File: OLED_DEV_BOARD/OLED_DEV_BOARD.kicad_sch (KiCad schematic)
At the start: 32 parts, among them J1 Barrel_Jack, J2 Conn_02x10_Odd_Even, J3 AudioJack3_Ground, J4 Conn_02x20_Odd_Even, SW1 SW_DIP_x02, SW2 SW_MEC_5E, SW3 SW_MEC_5E, SW4 SW_MEC_5E, SW5 SW_MEC_5E, SW6 SW_MEC_5E, SW7 SW_MEC_5E, U1 IS66WVS1M8BLL-104NLI, U2 W25Q32JVSS, U3 NCP1117-3.3_TO252

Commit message: Added proper footprint for OLED module and placed components roughly
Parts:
- J2: footprint Connector_PinHeader_2.54mm:PinHeader_2x10_P2.54mm_Vertical -> OLED:NHD-1.8-160128UBC3
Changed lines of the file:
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@@
     (property "Reference" "J2" (id 0) (at 49.53 30.5902 0))
     (property "Value" "Conn_02x10_Odd_Even" (id 1) (at 49.53 33.1271 0))
-    (property "Footprint" "Connector_PinHeader_2.54mm:PinHeader_2x10_P2.54mm_Vertical" (id 2) (at 48.26 45.72 0)
+    (property "Footprint" "OLED:NHD-1.8-160128UBC3" (id 2) (at 48.26 45.72 0)
       (effects (font (size 1.27 1.27)) hide)
     )
@@
     )
     (path "/a17904b9-135e-4dae-ae20-401c7787de72"
-      (reference "J2") (unit 1) (value "Conn_02x10_Odd_Even") (footprint "Connector_PinHeader_2.54mm:PinHeader_2x10_P2.54mm_Vertical")
+      (reference "J2") (unit 1) (value "Conn_02x10_Odd_Even") (footprint "OLED:NHD-1.8-160128UBC3")
     )
     (path "/97d5cdb2-e749-4919-9dcf-4b58ea280295"

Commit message: Made board smaller
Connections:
- net FLASH_CLK: now also J4.36 (Pin_36); no longer J4.32 (Pin_32)
- net FLASH_CSb: now also J4.32 (Pin_32); no longer J4.31 (Pin_31)
- net FLASH_D1: now also J4.31 (Pin_31); no longer J4.34 (Pin_34)
- net FLASH_D2: now also J4.34 (Pin_34); no longer J4.35 (Pin_35)
- net FLASH_D3: now also J4.35 (Pin_35); no longer J4.36 (Pin_36)
- net PSRAM_CLK: now also J4.24 (Pin_24); no longer J4.20 (Pin_20)
- net PSRAM_CSb: now also J4.20 (Pin_20); no longer J4.19 (Pin_19)
- net PSRAM_D1: now also J4.19 (Pin_19); no longer J4.22 (Pin_22)
- net PSRAM_D2: now also J4.22 (Pin_22); no longer J4.23 (Pin_23)
- net PSRAM_D3: now also J4.23 (Pin_23); no longer J4.24 (Pin_24)
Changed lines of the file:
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@@
-    (effects (font (size 1.27 1.27)) (justify left bottom))
-  )
-  (label "PSRAM_D2" (at 163.83 66.04 0)
     (effects (font (size 1.27 1.27)) (justify left bottom))
   )
@@
     (effects (font (size 1.27 1.27)) (justify left bottom))
   )
-  (label "GND" (at 30.48 35.56 0)
+  (label "PSRAM_CLK" (at 228.6 66.04 0)
     (effects (font (size 1.27 1.27)) (justify left bottom))
   )
-  (label "PSRAM_CSb" (at 163.83 60.96 0)
+  (label "FLASH_D3" (at 163.83 81.28 0)
+    (effects (font (size 1.27 1.27)) (justify left bottom))
+  )
+  (label "GND" (at 30.48 35.56 0)
     (effects (font (size 1.27 1.27)) (justify left bottom))
   )
@@
   )
   (label "DB7" (at 228.6 53.34 0)
+    (effects (font (size 1.27 1.27)) (justify left bottom))
+  )
+  (label "PSRAM_D1" (at 163.83 60.96 0)
     (effects (font (size 1.27 1.27)) (justify left bottom))
   )
@@
     (effects (font (size 1.27 1.27)) (justify left bottom))
   )
-  (label "FLASH_D3" (at 223.52 81.28 0)
-    (effects (font (size 1.27 1.27)) (justify left bottom))
-  )
   (label "RIGHT_BUTTON" (at 215.9 134.62 0)
     (effects (font (size 1.27 1.27)) (justify left bottom))
@@
     (effects (font (size 1.27 1.27)) (justify left bottom))
   )
-  (label "BS2" (at 144.78 68.58 0)
+  (label "PSRAM_D2" (at 228.6 63.5 0)
     (effects (font (size 1.27 1.27)) (justify left bottom))
   )
-  (label "PSRAM_CLK" (at 223.52 60.96 0)
+  (label "BS2" (at 144.78 68.58 0)
     (effects (font (size 1.27 1.27)) (justify left bottom))
   )
@@
     (effects (font (size 1.27 1.27)) (justify left bottom))
   )
+  (label "FLASH_CLK" (at 223.52 81.28 0)
+    (effects (font (size 1.27 1.27)) (justify left bottom))
+  )
   (label "DOWN_BUTTON" (at 223.52 71.12 0)
     (effects (font (size 1.27 1.27)) (justify left bottom))
@@
     (effects (font (size 1.27 1.27)) (justify left bottom))
   )
+  (label "FLASH_D1" (at 163.83 76.2 0)
+    (effects (font (size 1.27 1.27)) (justify left bottom))
+  )
   (label "FLASH_CSb" (at 26.67 115.57 0)
     (effects (font (size 1.27 1.27)) (justify left bottom))
   )
-  (label "PSRAM_D1" (at 223.52 63.5 0)
+  (label "PSRAM_D3" (at 163.83 66.04 0)
     (effects (font (size 1.27 1.27)) (justify left bottom))
   )
   (label "PSRAM_D3" (at 64.77 86.36 0)
-    (effects (font (size 1.27 1.27)) (justify left bottom))
-  )
-  (label "PSRAM_D3" (at 223.52 66.04 0)
     (effects (font (size 1.27 1.27)) (justify left bottom))
   )
@@
     (effects (font (size 1.27 1.27)) (justify left bottom))
   )
-  (label "FLASH_D1" (at 223.52 78.74 0)
-    (effects (font (size 1.27 1.27)) (justify left bottom))
-  )
   (label "DB6" (at 29.21 50.8 0)
-    (effects (font (size 1.27 1.27)) (justify left bottom))
-  )
-  (label "FLASH_CSb" (at 163.83 76.2 0)
     (effects (font (size 1.27 1.27)) (justify left bottom))
   )
@@
   )
   (label "UP_BUTTON" (at 191.77 118.11 0)
-    (effects (font (size 1.27 1.27)) (justify left bottom))
-  )
-  (label "FLASH_D2" (at 163.83 81.28 0)
     (effects (font (size 1.27 1.27)) (justify left bottom))
   )
@@
     (effects (font (size 1.27 1.27)) (justify left bottom))
   )
+  (label "FLASH_D2" (at 223.52 78.74 0)
+    (effects (font (size 1.27 1.27)) (justify left bottom))
+  )
   (label "DB2" (at 163.83 48.26 0)
     (effects (font (size 1.27 1.27)) (justify left bottom))
   )
   (label "E" (at 163.83 43.18 0)
-    (effects (font (size 1.27 1.27)) (justify left bottom))
-  )
-  (label "FLASH_CLK" (at 223.52 76.2 0)
     (effects (font (size 1.27 1.27)) (justify left bottom))
   )
@@
     (effects (font (size 1.27 1.27)) (justify left bottom))
   )
+  (label "FLASH_CSb" (at 223.52 76.2 0)
+    (effects (font (size 1.27 1.27)) (justify left bottom))
+  )
   (label "DB4" (at 29.21 48.26 0)
     (effects (font (size 1.27 1.27)) (justify left bottom))
@@
     (effects (font (size 1.27 1.27)) (justify left bottom))
   )
+  (label "PSRAM_CSb" (at 228.6 60.96 0)
+    (effects (font (size 1.27 1.27)) (justify left bottom))
+  )

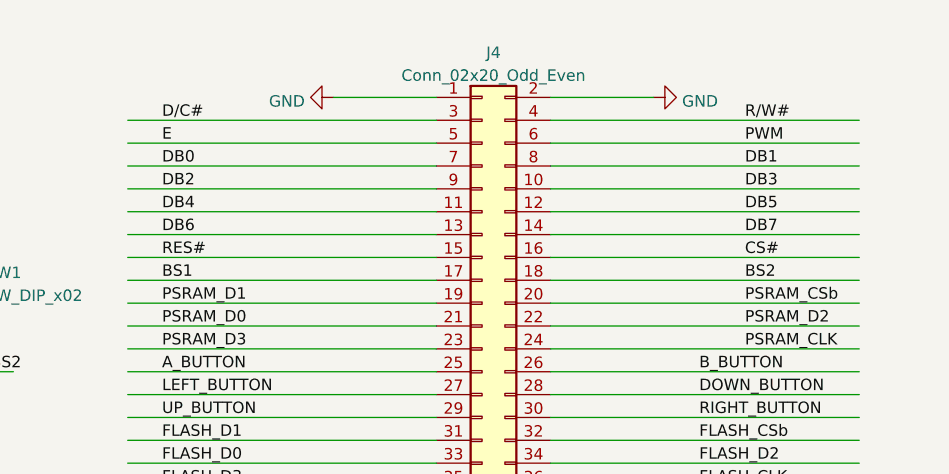
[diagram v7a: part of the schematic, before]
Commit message: Changed ordering of pins for display so it would route better
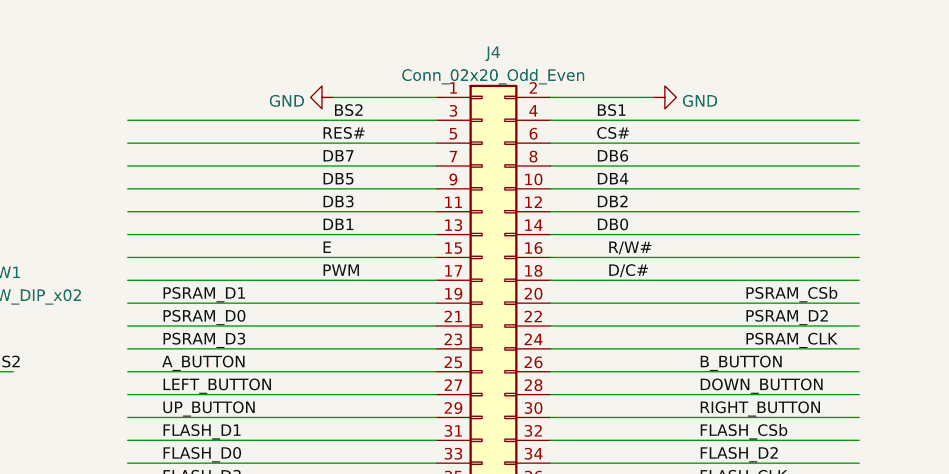
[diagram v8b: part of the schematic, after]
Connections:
- net BS1: now also J4.4 (Pin_4); no longer J4.17 (Pin_17)
- net BS2: now also J4.3 (Pin_3); no longer J4.18 (Pin_18)
- net CS#: now also J4.6 (Pin_6); no longer J4.16 (Pin_16)
- net DB0: now also J4.14 (Pin_14); no longer J4.7 (Pin_7)
- net DB1: now also J4.13 (Pin_13); no longer J4.8 (Pin_8)
- net DB2: now also J4.12 (Pin_12); no longer J4.9 (Pin_9)
- net DB3: now also J4.11 (Pin_11); no longer J4.10 (Pin_10)
- net DB4: now also J4.10 (Pin_10); no longer J4.11 (Pin_11)
- net DB5: now also J4.9 (Pin_9); no longer J4.12 (Pin_12)
- net DB6: now also J4.8 (Pin_8); no longer J4.13 (Pin_13)
- net DB7: now also J4.7 (Pin_7); no longer J4.14 (Pin_14)
- net D/C#: now also J4.18 (Pin_18); no longer J4.3 (Pin_3)
- net E: now also J4.15 (Pin_15); no longer J4.5 (Pin_5)
- net PWM: now also J4.17 (Pin_17); no longer J4.6 (Pin_6)
- net RES#: now also J4.5 (Pin_5); no longer J4.15 (Pin_15)
- net R/W#: now also J4.16 (Pin_16); no longer J4.4 (Pin_4)
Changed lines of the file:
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@@
-    (effects (font (size 1.27 1.27)) (justify left bottom))
-  )
-  (label "DB4" (at 163.83 50.8 0)
     (effects (font (size 1.27 1.27)) (justify left bottom))
   )
@@
     (effects (font (size 1.27 1.27)) (justify left bottom))
   )
-  (label "BS2" (at 228.6 58.42 0)
-    (effects (font (size 1.27 1.27)) (justify left bottom))
-  )
-  (label "CS#" (at 228.6 55.88 0)
-    (effects (font (size 1.27 1.27)) (justify left bottom))
-  )
   (label "FLASH_D0" (at 67.31 113.03 0)
     (effects (font (size 1.27 1.27)) (justify left bottom))
@@
     (effects (font (size 1.27 1.27)) (justify left bottom))
   )
-  (label "D{slash}C#" (at 163.83 40.64 0)
-    (effects (font (size 1.27 1.27)) (justify left bottom))
-  )
-  (label "DB7" (at 228.6 53.34 0)
-    (effects (font (size 1.27 1.27)) (justify left bottom))
-  )
   (label "PSRAM_D1" (at 163.83 60.96 0)
     (effects (font (size 1.27 1.27)) (justify left bottom))
@@
     (effects (font (size 1.27 1.27)) (justify left bottom))
   )
+  (label "R{slash}W#" (at 213.36 55.88 0)
+    (effects (font (size 1.27 1.27)) (justify left bottom))
+  )
   (label "RIGHT_BUTTON" (at 215.9 134.62 0)
     (effects (font (size 1.27 1.27)) (justify left bottom))
   )
-  (label "BS1" (at 163.83 58.42 0)
-    (effects (font (size 1.27 1.27)) (justify left bottom))
-  )
-  (label "RES#" (at 163.83 55.88 0)
-    (effects (font (size 1.27 1.27)) (justify left bottom))
-  )
   (label "PSRAM_D2" (at 228.6 63.5 0)
     (effects (font (size 1.27 1.27)) (justify left bottom))
@@
     (effects (font (size 1.27 1.27)) (justify left bottom))
   )
+  (label "DB4" (at 212.09 48.26 0)
+    (effects (font (size 1.27 1.27)) (justify left bottom))
+  )
+  (label "PWM" (at 181.61 58.42 0)
+    (effects (font (size 1.27 1.27)) (justify left bottom))
+  )
   (label "PSRAM_CSb" (at 27.94 83.82 0)
     (effects (font (size 1.27 1.27)) (justify left bottom))
@@
     (effects (font (size 1.27 1.27)) (justify left bottom))
   )
+  (label "DB7" (at 181.61 45.72 0)
+    (effects (font (size 1.27 1.27)) (justify left bottom))
+  )
+  (label "RES#" (at 181.61 43.18 0)
+    (effects (font (size 1.27 1.27)) (justify left bottom))
+  )
   (label "DOWN_BUTTON" (at 223.52 71.12 0)
     (effects (font (size 1.27 1.27)) (justify left bottom))
@@
     (effects (font (size 1.27 1.27)) (justify left bottom))
   )
+  (label "DB1" (at 181.61 53.34 0)
+    (effects (font (size 1.27 1.27)) (justify left bottom))
+  )
   (label "PSRAM_CLK" (at 64.77 88.9 0)
     (effects (font (size 1.27 1.27)) (justify left bottom))
@@
     (effects (font (size 1.27 1.27)) (justify left bottom))
   )
+  (label "E" (at 181.61 55.88 0)
+    (effects (font (size 1.27 1.27)) (justify left bottom))
+  )
   (label "PSRAM_D3" (at 64.77 86.36 0)
     (effects (font (size 1.27 1.27)) (justify left bottom))
@@
     (effects (font (size 1.27 1.27)) (justify left bottom))
   )
+  (label "D{slash}C#" (at 213.36 58.42 0)
+    (effects (font (size 1.27 1.27)) (justify left bottom))
+  )
   (label "DB3" (at 62.23 45.72 0)
     (effects (font (size 1.27 1.27)) (justify left bottom))
@@
     (effects (font (size 1.27 1.27)) (justify left bottom))
   )
-  (label "DB1" (at 228.6 45.72 0)
-    (effects (font (size 1.27 1.27)) (justify left bottom))
-  )
   (label "A_BUTTON" (at 158.75 119.38 0)
     (effects (font (size 1.27 1.27)) (justify left bottom))
@@
     (effects (font (size 1.27 1.27)) (justify left bottom))
   )
-  (label "DB0" (at 163.83 45.72 0)
+  (label "BS1" (at 212.09 40.64 0)
     (effects (font (size 1.27 1.27)) (justify left bottom))
   )
@@
     (effects (font (size 1.27 1.27)) (justify left bottom))
   )
+  (label "DB2" (at 212.09 50.8 0)
+    (effects (font (size 1.27 1.27)) (justify left bottom))
+  )
   (label "DB5" (at 62.23 48.26 0)
     (effects (font (size 1.27 1.27)) (justify left bottom))
   )
-  (label "R{slash}W#" (at 228.6 40.64 0)
-    (effects (font (size 1.27 1.27)) (justify left bottom))
-  )
   (label "FLASH_CLK" (at 26.67 120.65 0)
     (effects (font (size 1.27 1.27)) (justify left bottom))
@@
     (effects (font (size 1.27 1.27)) (justify left bottom))
   )
-  (label "DB2" (at 163.83 48.26 0)
-    (effects (font (size 1.27 1.27)) (justify left bottom))
-  )
-  (label "E" (at 163.83 43.18 0)
-    (effects (font (size 1.27 1.27)) (justify left bottom))
-  )
-  (label "DB5" (at 228.6 50.8 0)
+  (label "DB5" (at 181.61 48.26 0)
     (effects (font (size 1.27 1.27)) (justify left bottom))
   )
@@
     (effects (font (size 1.27 1.27)) (justify left bottom))
   )
+  (label "CS#" (at 212.09 43.18 0)
+    (effects (font (size 1.27 1.27)) (justify left bottom))
+  )
+  (label "DB0" (at 212.09 53.34 0)
+    (effects (font (size 1.27 1.27)) (justify left bottom))
+  )
+  (label "DB6" (at 212.09 45.72 0)
+    (effects (font (size 1.27 1.27)) (justify left bottom))
+  )
   (label "CS#" (at 29.21 55.88 0)
     (effects (font (size 1.27 1.27)) (justify left bottom))
@@
     (effects (font (size 1.27 1.27)) (justify left bottom))
   )
-  (label "PWM" (at 228.6 43.18 0)
-    (effects (font (size 1.27 1.27)) (justify left bottom))
-  )
   (label "LEFT_BUTTON" (at 163.83 71.12 0)
     (effects (font (size 1.27 1.27)) (justify left bottom))
@@
     (effects (font (size 1.27 1.27)) (justify left bottom))
   )
+  (label "BS2" (at 182.88 40.64 0)
+    (effects (font (size 1.27 1.27)) (justify left bottom))
+  )
   (label "DB4" (at 29.21 48.26 0)
     (effects (font (size 1.27 1.27)) (justify left bottom))
   )
-  (label "DB3" (at 228.6 48.26 0)
-    (effects (font (size 1.27 1.27)) (justify left bottom))
-  )
   (label "BS2" (at 62.23 58.42 0)
     (effects (font (size 1.27 1.27)) (justify left bottom))
@@
     (effects (font (size 1.27 1.27)) (justify left bottom))
   )
+  (label "DB3" (at 181.61 50.8 0)
+    (effects (font (size 1.27 1.27)) (justify left bottom))
+  )
   (label "BS1" (at 29.21 58.42 0)
     (effects (font (size 1.27 1.27)) (justify left bottom))
   )
-  (label "DB6" (at 163.83 53.34 0)
-    (effects (font (size 1.27 1.27)) (justify left bottom))
-  )
